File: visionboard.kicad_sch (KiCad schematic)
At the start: 1 part, among them U1 Hirose DF40C-100DS-0.4V

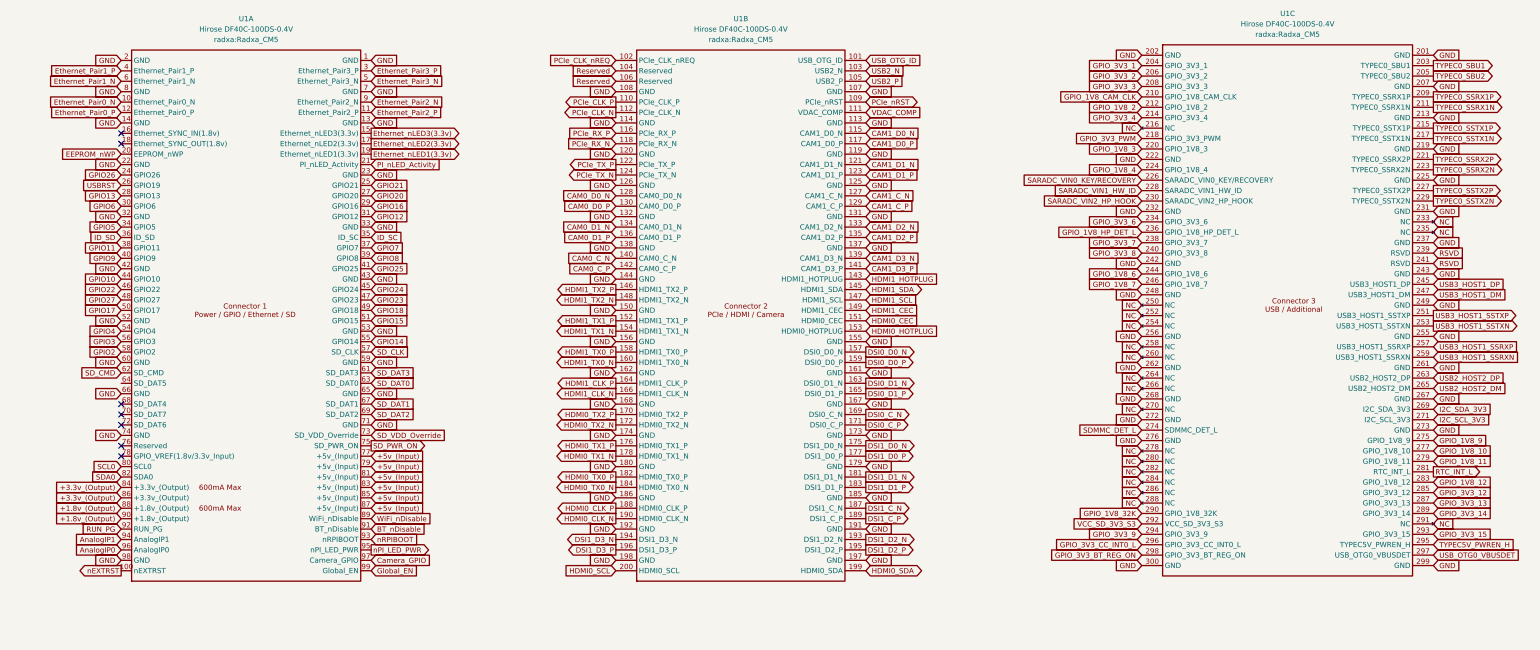
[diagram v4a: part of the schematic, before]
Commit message: finished usb3.0
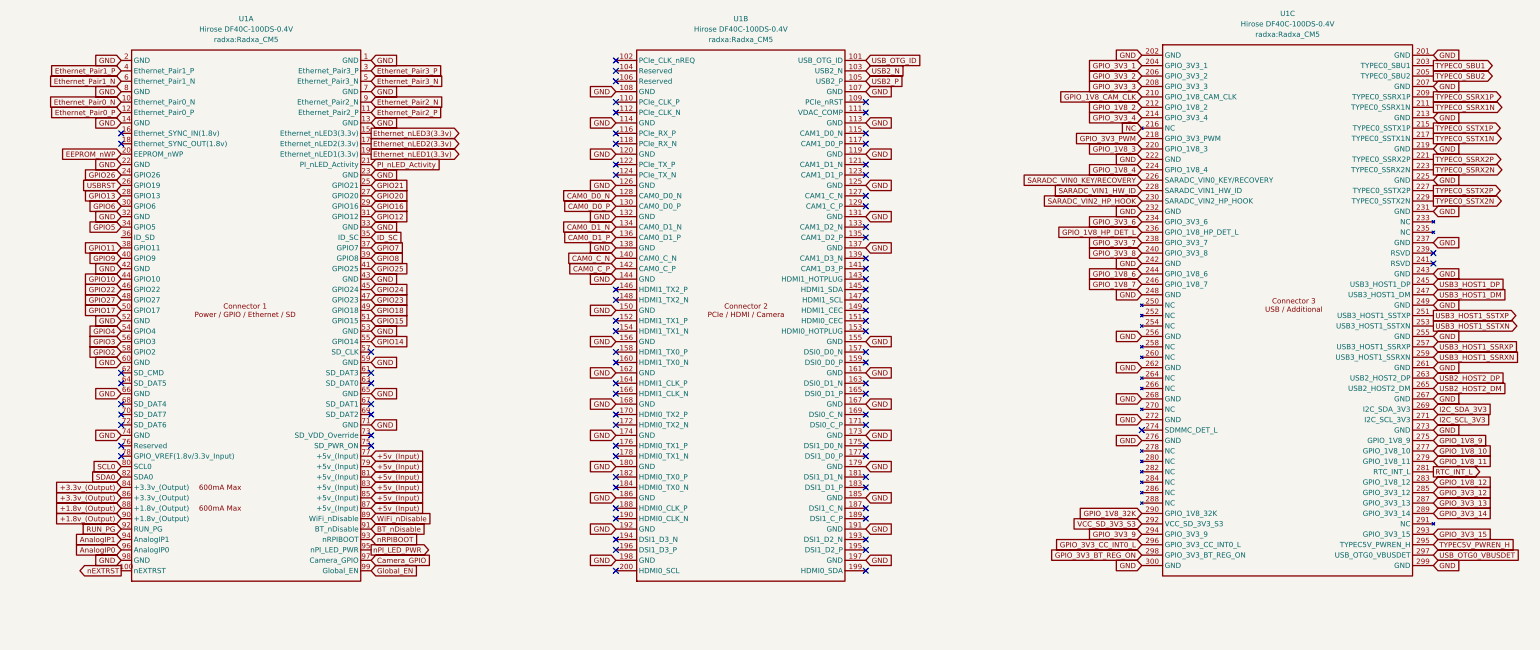
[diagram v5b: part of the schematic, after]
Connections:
- net NC: no longer U1.233 (NC), U1.235 (NC), U1.250 (NC), U1.252 (NC), U1.254 (NC), U1.258 (NC), U1.260 (NC), U1.264 (NC), U1.266 (NC), U1.270 (NC), U1.278 (NC), U1.280 (NC), U1.282 (NC), U1.284 (NC), U1.286 (NC), U1.288 (NC), U1.291 (NC)
- net CAM1_C_N: no longer names the net of U1.127 (CAM1_C_N)
- net CAM1_C_P: no longer names the net of U1.129 (CAM1_C_P)
- net CAM1_D0_N: no longer names the net of U1.115 (CAM1_D0_N)
- net CAM1_D0_P: no longer names the net of U1.117 (CAM1_D0_P)
- net CAM1_D1_N: no longer names the net of U1.121 (CAM1_D1_N)
- net CAM1_D1_P: no longer names the net of U1.123 (CAM1_D1_P)
- net CAM1_D2_N: no longer names the net of U1.133 (CAM1_D2_N)
- net CAM1_D2_P: no longer names the net of U1.135 (CAM1_D2_P)
- net CAM1_D3_N: no longer names the net of U1.139 (CAM1_D3_N)
- net CAM1_D3_P: no longer names the net of U1.141 (CAM1_D3_P)
- net DSI0_C_N: no longer names the net of U1.169 (DSI0_C_N)
- net DSI0_C_P: no longer names the net of U1.171 (DSI0_C_P)
- net DSI0_D0_N: no longer names the net of U1.157 (DSI0_D0_N)
- net DSI0_D0_P: no longer names the net of U1.159 (DSI0_D0_P)
- net DSI0_D1_N: no longer names the net of U1.163 (DSI0_D1_N)
- net DSI0_D1_P: no longer names the net of U1.165 (DSI0_D1_P)
- net DSI1_C_N: no longer names the net of U1.187 (DSI1_C_N)
- net DSI1_C_P: no longer names the net of U1.189 (DSI1_C_P)
- net DSI1_D0_N: no longer names the net of U1.175 (DSI1_D0_N)
- net DSI1_D0_P: no longer names the net of U1.177 (DSI1_D0_P)
- net DSI1_D1_N: no longer names the net of U1.181 (DSI1_D1_N)
- net DSI1_D1_P: no longer names the net of U1.183 (DSI1_D1_P)
- net DSI1_D2_N: no longer names the net of U1.193 (DSI1_D2_N)
- net DSI1_D2_P: no longer names the net of U1.195 (DSI1_D2_P)
- net DSI1_D3_N: no longer names the net of U1.194 (DSI1_D3_N)
- net DSI1_D3_P: no longer names the net of U1.196 (DSI1_D3_P)
- net HDMI0_CEC: no longer names the net of U1.151 (HDMI0_CEC)
- net HDMI0_CLK_N: no longer names the net of U1.190 (HDMI0_CLK_N)
- net HDMI0_CLK_P: no longer names the net of U1.188 (HDMI0_CLK_P)
- net HDMI0_HOTPLUG: no longer names the net of U1.153 (HDMI0_HOTPLUG)
- net HDMI0_SCL: no longer names the net of U1.200 (HDMI0_SCL)
- net HDMI0_SDA: no longer names the net of U1.199 (HDMI0_SDA)
- net HDMI0_TX0_N: no longer names the net of U1.184 (HDMI0_TX0_N)
- net HDMI0_TX0_P: no longer names the net of U1.182 (HDMI0_TX0_P)
- net HDMI0_TX1_N: no longer names the net of U1.178 (HDMI0_TX1_N)
- net HDMI0_TX1_P: no longer names the net of U1.176 (HDMI0_TX1_P)
- net HDMI0_TX2_N: no longer names the net of U1.172 (HDMI0_TX2_N)
- net HDMI0_TX2_P: no longer names the net of U1.170 (HDMI0_TX2_P)
- net HDMI1_CEC: no longer names the net of U1.149 (HDMI1_CEC)
- net HDMI1_CLK_N: no longer names the net of U1.166 (HDMI1_CLK_N)
- net HDMI1_CLK_P: no longer names the net of U1.164 (HDMI1_CLK_P)
- net HDMI1_HOTPLUG: no longer names the net of U1.143 (HDMI1_HOTPLUG)
- net HDMI1_SCL: no longer names the net of U1.147 (HDMI1_SCL)
- net HDMI1_SDA: no longer names the net of U1.145 (HDMI1_SDA)
- net HDMI1_TX0_N: no longer names the net of U1.160 (HDMI1_TX0_N)
- net HDMI1_TX0_P: no longer names the net of U1.158 (HDMI1_TX0_P)
- net HDMI1_TX1_N: no longer names the net of U1.154 (HDMI1_TX1_N)
- net HDMI1_TX1_P: no longer names the net of U1.152 (HDMI1_TX1_P)
- net HDMI1_TX2_N: no longer names the net of U1.148 (HDMI1_TX2_N)
- net HDMI1_TX2_P: no longer names the net of U1.146 (HDMI1_TX2_P)
- net ID_SD: no longer names the net of U1.36 (ID_SD)
- net PCIe_CLK_N: no longer names the net of U1.112 (PCIe_CLK_N)
- net PCIe_CLK_P: no longer names the net of U1.110 (PCIe_CLK_P)
- net PCIe_CLK_nREQ: no longer names the net of U1.102 (PCIe_CLK_nREQ)
- net PCIe_RX_N: no longer names the net of U1.118 (PCIe_RX_N)
- net PCIe_RX_P: no longer names the net of U1.116 (PCIe_RX_P)
- net PCIe_TX_N: no longer names the net of U1.124 (PCIe_TX_N)
- net PCIe_TX_P: no longer names the net of U1.122 (PCIe_TX_P)
- net PCIe_nRST: no longer names the net of U1.109 (PCIe_nRST)
- net RSVD: no longer names the net of U1.239 (RSVD)
- net RSVD: no longer U1.241 (RSVD)
- net Reserved: no longer names the net of U1.104 (Reserved)
- net Reserved: no longer U1.106 (Reserved)
- net SDMMC_DET_L: no longer names the net of U1.274 (SDMMC_DET_L)
- net SD_CLK: no longer names the net of U1.57 (SD_CLK)
- net SD_CMD: no longer names the net of U1.62 (SD_CMD)
- net SD_DAT0: no longer names the net of U1.63 (SD_DAT0)
- net SD_DAT1: no longer names the net of U1.67 (SD_DAT1)
- net SD_DAT2: no longer names the net of U1.69 (SD_DAT2)
- net SD_DAT3: no longer names the net of U1.61 (SD_DAT3)
- net SD_PWR_ON: no longer names the net of U1.75 (SD_PWR_ON)
- net SD_VDD_Override: no longer names the net of U1.73 (SD_VDD_Override)
- net VDAC_COMP: no longer names the net of U1.111 (VDAC_COMP)
- no-connect marks 7 -> 80

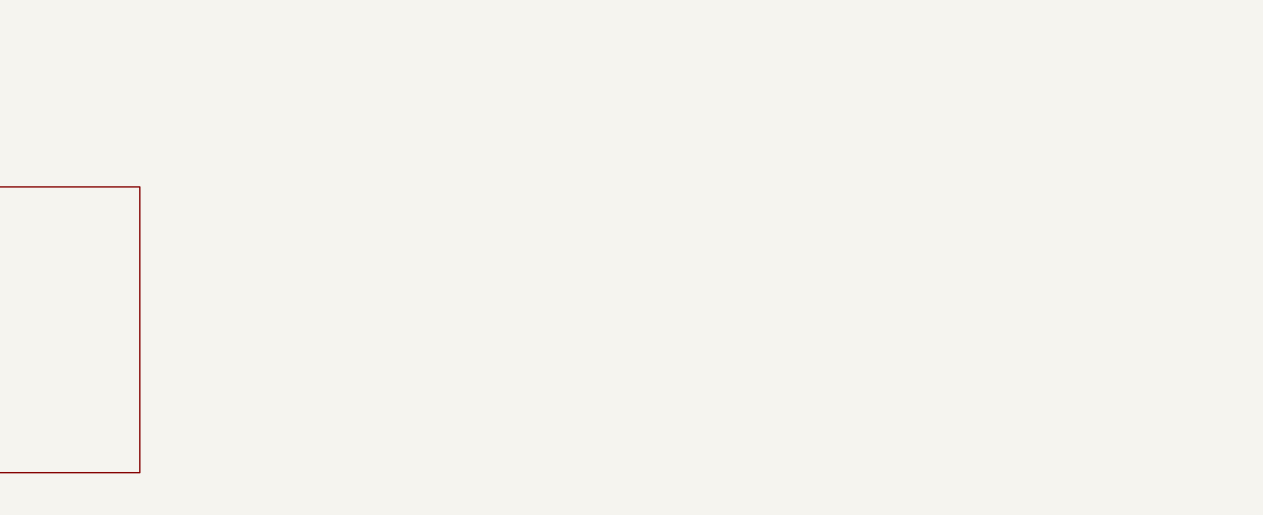
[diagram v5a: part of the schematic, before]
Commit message: Ethernet and MIPI cam done, USBC OTG started
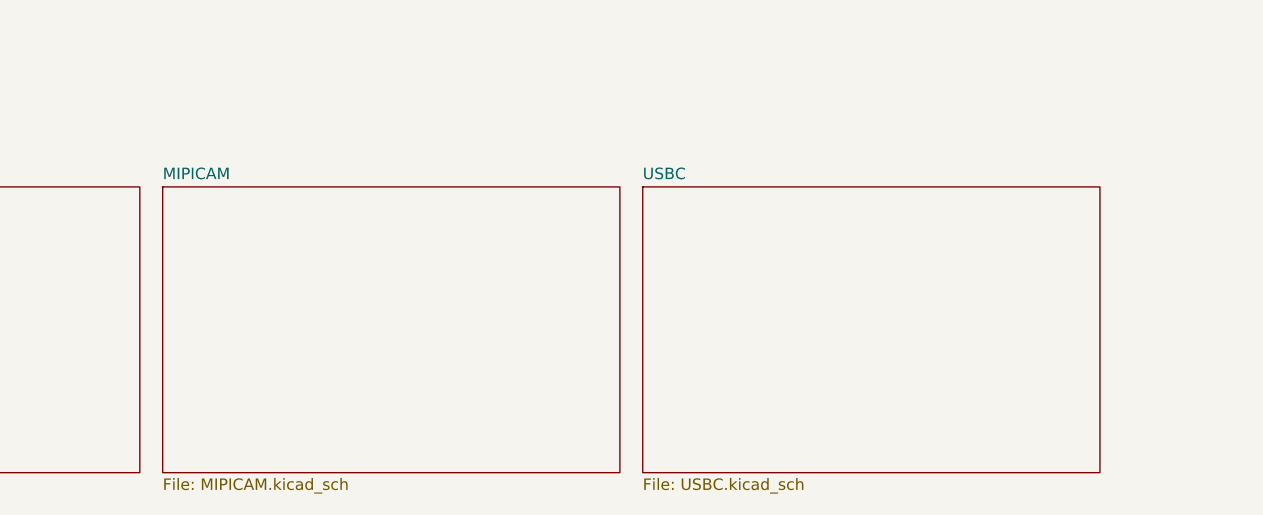
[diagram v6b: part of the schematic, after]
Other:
- added sheet MIPICAM (MIPICAM.kicad_sch)
- added sheet USBC (USBC.kicad_sch)
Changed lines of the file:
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@@
+	)
+	(sheet
+		(at 252.73 304.8)
+		(size 50.8 31.75)
+		(exclude_from_sim no)
+		(in_bom yes)
+		(on_board yes)
+		(dnp no)
+		(fields_autoplaced yes)
+		(stroke
+			(width 0.1524)
+			(type solid)
+		)
+		(fill
+			(color 0 0 0 0.0000)
+		)
+		(property "Sheetname" "MIPICAM"
+			(at 252.73 304.0884 0)
+			(effects
+				(font
+					(size 1.27 1.27)
+				)
+				(justify left bottom)
+			)
+		)
+		(property "Sheetfile" "MIPICAM.kicad_sch"
+			(at 252.73 337.1346 0)
+			(effects
+				(font
+					(size 1.27 1.27)
+				)
+				(justify left top)
+			)
+		)
+		(instances
+			(project "visionboard"
+				(path "/600da949-f681-489f-915b-075a1ebe377b"
+					(page "11")
+				)
+			)
+		)
 	)
 	(sheet
@@
 				)
 			)
+		)
+	)
+	(sheet
+		(at 306.07 304.8)
+		(size 50.8 31.75)
+		(exclude_from_sim no)
+		(in_bom yes)
+		(on_board yes)
+		(dnp no)
+		(fields_autoplaced yes)
+		(stroke
+			(width 0.1524)
+			(type solid)
+		)
+		(fill
+			(color 0 0 0 0.0000)
+		)
+		(property "Sheetname" "USBC"
+			(at 306.07 304.0884 0)
+			(effects
+				(font
+					(size 1.27 1.27)
+				)
+				(justify left bottom)
+			)
+		)
+		(property "Sheetfile" "USBC.kicad_sch"
+			(at 306.07 337.1346 0)
+			(effects
+				(font
+					(size 1.27 1.27)
+				)
+				(justify left top)
+			)
+		)
+		(instances
+			(project "visionboard"
+				(path "/600da949-f681-489f-915b-075a1ebe377b"
+					(page "12")
+				)
+			)

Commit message: usbc work
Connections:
- net USB_OTG_ID: no longer names the net of U1.101 (USB_OTG_ID)
- no-connect marks 80 -> 81
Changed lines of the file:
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@@
 	)
 	(no_connect
-		(at 364.49 120.65)
+		(at 226.06 71.12)
 	)
 	(no_connect
-		(at 165.1 91.44)
+		(at 364.49 120.65)
 	)
 	(no_connect
-		(at 165.1 76.2)
+		(at 165.1 91.44)
 	)
 	(no_connect
@@
 	)
 	(no_connect
+		(at 165.1 76.2)
+	)
+	(no_connect
 		(at 226.06 124.46)
 	)
@@
 			(effects
 				(font
-					(size 1.27 1.27)
-				)
-				(hide yes)
-			)
-		)
-	)
-	(global_label "USB_OTG_ID"
-		(shape input)
-		(at 226.06 71.12 0)
-		(effects
-			(font
-				(size 1.27 1.27)
-			)
-			(justify left)
-		)
-		(property "Intersheetrefs" "${INTERSHEET_REFS}"
-			(at 226.06 71.12 0)
-			(effects
-				(font

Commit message: usbc work
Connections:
- net VCC5V0_SYS: now reaches U1.106 (Reserved)
- net USB_OTG0_VBUSDET: no longer names the net of U1.297 (USB_OTG0_VBUSDET)
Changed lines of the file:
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@@
+	)
+	(no_connect
+		(at 364.49 191.77)
 	)
 	(no_connect
@@
 	(no_connect
 		(at 165.1 167.64)
-	)
-	(no_connect
-		(at 165.1 76.2)
 	)
 	(no_connect
@@
 		)
 	)
-	(global_label "USB_OTG0_VBUSDET"
-		(shape input)
-		(at 364.49 191.77 0)
-		(effects
-			(font
-				(size 1.27 1.27)
-			)
-			(justify left)
-		)
-		(property "Intersheetrefs" "${INTERSHEET_REFS}"
-			(at 364.49 191.77 0)
-			(effects
-				(font
-					(size 1.27 1.27)
-				)
-				(hide yes)
-			)
-		)
-	)
 	(global_label "+5v_(Input)"
 		(shape input)
@@
 				(hide yes)
 			)
+		)
+	)
+	(global_label "VCC5V0_SYS"
+		(shape input)
+		(at 165.1 76.2 180)
+		(fields_autoplaced yes)
+		(effects
+			(font
+				(size 1.27 1.27)
+			)
+			(justify right)
+		)
+		(property "Intersheetrefs" "${INTERSHEET_REFS}"
+			(at 150.5034 76.2 0)
+			(effects
+				(font
+					(size 1.27 1.27)
+				)
+				(justify right)
+				(hide yes)
+			)
